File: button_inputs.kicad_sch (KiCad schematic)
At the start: 0 parts

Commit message: Add schematic for button inputs and I2C signal busses.
* Define 9x button inputs
* Define I2C parallel bus expanders used for FET output signals
  and button inputs
* Add (empty) schematic for 5V switching regulator.
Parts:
- added R? (x18): (no value), symbol Device:R_Small
- added SW? (x9): (no value), symbol Switch:SW_SPST
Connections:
- new net: R?.2, SW?.1 (A) (x9)
- new net GND: R?.1, R?.1, R?.1, R?.1, R?.1, R?.1, R?.1, R?.1, R?.1
- new net VCC: R?.1, R?.1, R?.1, R?.1, R?.1, R?.1, R?.1, R?.1, R?.1
- new net button0: R?.2, SW?.2 (B)
- new net button1: R?.2, SW?.2 (B)
- new net button2: R?.2, SW?.2 (B)
- new net button3: R?.2, SW?.2 (B)
- new net button4: R?.2, SW?.2 (B)
- new net button5: R?.2, SW?.2 (B)
- new net button6: R?.2, SW?.2 (B)
- new net button7: R?.2
- new net button8: R?.2, SW?.2 (B)
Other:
- note added: "3V3 logic through buttons"
- note added: "All buttons are active-low, normally-open circuit"

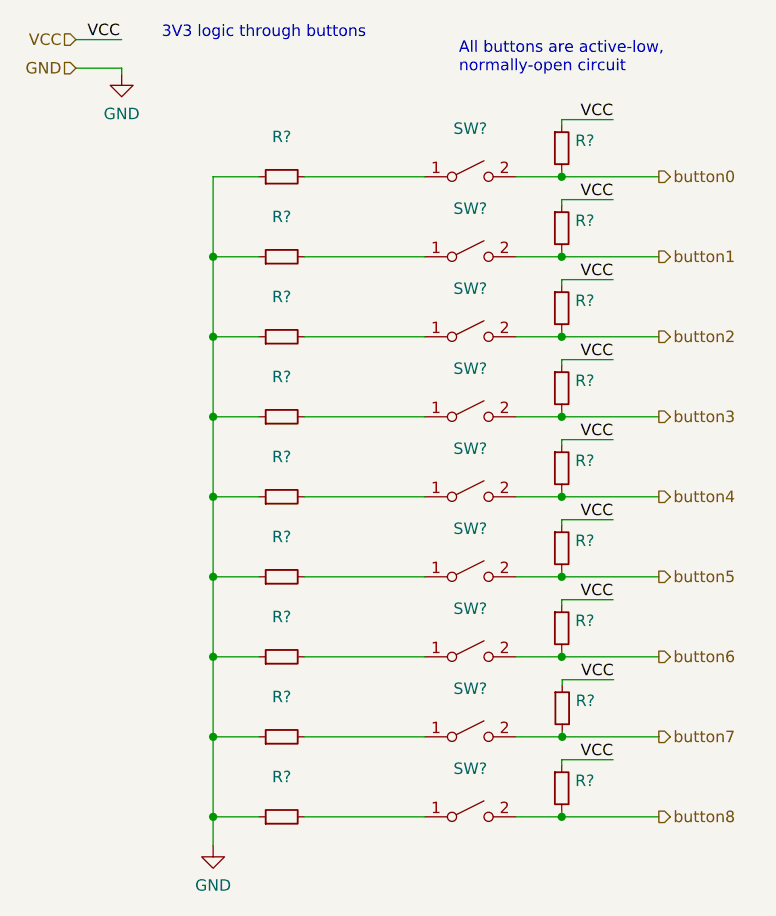
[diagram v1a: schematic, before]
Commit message: Sketch out ISL8117-driven 12V regulator.
Another candidate entry for on-board 12V regulation is to
build our own based on the reference schematic from the ISL8117
DC buck regulator controller datasheet.

Implemented (most of) this reference schematic here.
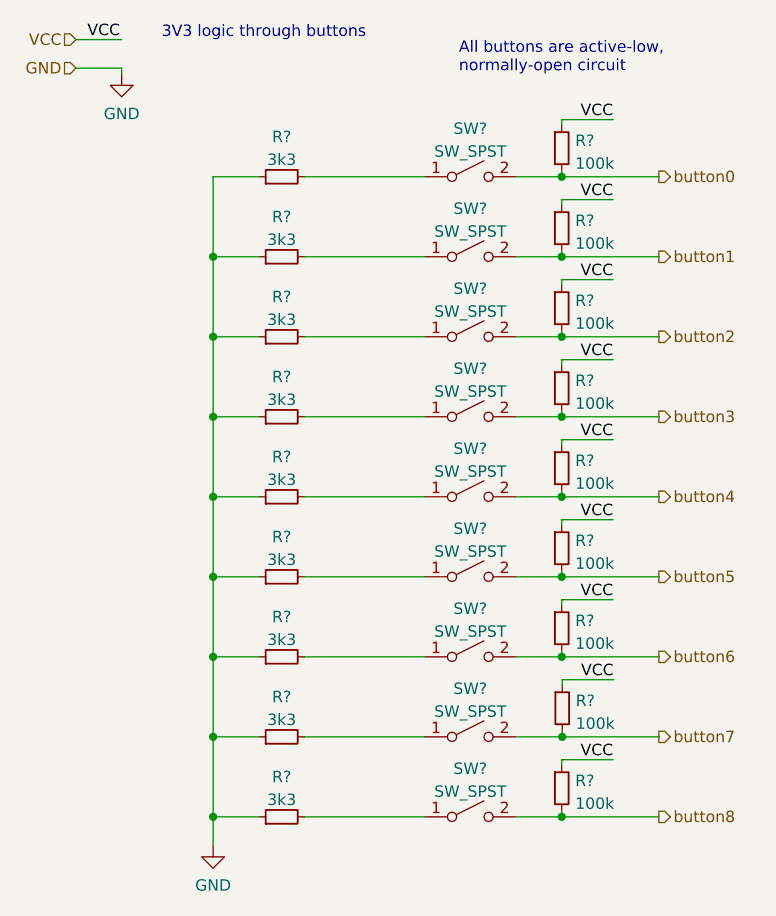
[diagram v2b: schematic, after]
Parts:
- R? (x9): value (none) -> 100k
- R? (x9): value (none) -> 3k3
- SW? (x9): value (none) -> SW_SPST
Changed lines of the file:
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@@
     (in_bom yes) (on_board yes) (fields_autoplaced)
     (property "Reference" "SW?" (id 0) (at 64.135 36.5592 0))
-    (property "Value" "" (id 1) (at 64.135 39.0961 0))
+    (property "Value" "SW_SPST" (id 1) (at 64.135 39.0961 0))
     (property "Footprint" "" (id 2) (at 64.135 41.91 0)
       (effects (font (size 1.27 1.27)) hide)
@@
       (effects (font (size 1.27 1.27)) (justify left))
     )
-    (property "Value" "" (id 1) (at 75.7936 49.3272 0)
+    (property "Value" "100k" (id 1) (at 75.7936 49.3272 0)
       (effects (font (size 1.27 1.27)) (justify left))
     )
@@
     (in_bom yes) (on_board yes)
     (property "Reference" "R?" (id 0) (at 43.18 37.4736 90))
-    (property "Value" "" (id 1) (at 43.18 40.0105 90))
+    (property "Value" "3k3" (id 1) (at 43.18 40.0105 90))
     (property "Footprint" "" (id 2) (at 43.18 41.91 0)
       (effects (font (size 1.27 1.27)) hide)
@@
     (in_bom yes) (on_board yes)
     (property "Reference" "R?" (id 0) (at 43.18 81.9236 90))
-    (property "Value" "" (id 1) (at 43.18 84.4605 90))
+    (property "Value" "3k3" (id 1) (at 43.18 84.4605 90))
     (property "Footprint" "" (id 2) (at 43.18 86.36 0)
       (effects (font (size 1.27 1.27)) hide)
@@
       (effects (font (size 1.27 1.27)) (justify left))
     )
-    (property "Value" "" (id 1) (at 75.8487 93.7772 0)
+    (property "Value" "100k" (id 1) (at 75.8487 93.7772 0)
       (effects (font (size 1.27 1.27)) (justify left))
     )
@@
     (in_bom yes) (on_board yes)
     (property "Reference" "R?" (id 0) (at 43.18 64.1436 90))
-    (property "Value" "" (id 1) (at 43.18 66.6805 90))
+    (property "Value" "3k3" (id 1) (at 43.18 66.6805 90))
     (property "Footprint" "" (id 2) (at 43.18 68.58 0)
       (effects (font (size 1.27 1.27)) hide)
@@
       (effects (font (size 1.27 1.27)) (justify left))
     )
-    (property "Value" "" (id 1) (at 75.7936 40.4372 0)
+    (property "Value" "100k" (id 1) (at 75.7936 40.4372 0)
       (effects (font (size 1.27 1.27)) (justify left))
     )
@@
     (in_bom yes) (on_board yes) (fields_autoplaced)
     (property "Reference" "SW?" (id 0) (at 64.135 81.0092 0))
-    (property "Value" "" (id 1) (at 64.135 83.5461 0))
+    (property "Value" "SW_SPST" (id 1) (at 64.135 83.5461 0))
     (property "Footprint" "" (id 2) (at 64.135 86.36 0)
       (effects (font (size 1.27 1.27)) hide)
@@
     (in_bom yes) (on_board yes) (fields_autoplaced)
     (property "Reference" "SW?" (id 0) (at 64.135 45.4492 0))
-    (property "Value" "" (id 1) (at 64.135 47.9861 0))
+    (property "Value" "SW_SPST" (id 1) (at 64.135 47.9861 0))
     (property "Footprint" "" (id 2) (at 64.135 50.8 0)
       (effects (font (size 1.27 1.27)) hide)
@@
     (in_bom yes) (on_board yes)
     (property "Reference" "R?" (id 0) (at 43.18 55.2536 90))
-    (property "Value" "" (id 1) (at 43.18 57.7905 90))
+    (property "Value" "3k3" (id 1) (at 43.18 57.7905 90))
     (property "Footprint" "" (id 2) (at 43.18 59.69 0)
       (effects (font (size 1.27 1.27)) hide)
@@
     (in_bom yes) (on_board yes) (fields_autoplaced)
     (property "Reference" "SW?" (id 0) (at 64.135 54.3392 0))
-    (property "Value" "" (id 1) (at 64.135 56.8761 0))
+    (property "Value" "SW_SPST" (id 1) (at 64.135 56.8761 0))
     (property "Footprint" "" (id 2) (at 64.135 59.69 0)
       (effects (font (size 1.27 1.27)) hide)
@@
     (in_bom yes) (on_board yes) (fields_autoplaced)
     (property "Reference" "SW?" (id 0) (at 64.135 89.8992 0))
-    (property "Value" "" (id 1) (at 64.135 92.4361 0))
+    (property "Value" "SW_SPST" (id 1) (at 64.135 92.4361 0))
     (property "Footprint" "" (id 2) (at 64.135 95.25 0)
       (effects (font (size 1.27 1.27)) hide)
@@
     (in_bom yes) (on_board yes) (fields_autoplaced)
     (property "Reference" "SW?" (id 0) (at 64.135 72.1192 0))
-    (property "Value" "" (id 1) (at 64.135 74.6561 0))
+    (property "Value" "SW_SPST" (id 1) (at 64.135 74.6561 0))
     (property "Footprint" "" (id 2) (at 64.135 77.47 0)
       (effects (font (size 1.27 1.27)) hide)
@@
       (effects (font (size 1.27 1.27)) (justify left))
     )
-    (property "Value" "" (id 1) (at 75.7936 58.2172 0)
+    (property "Value" "100k" (id 1) (at 75.7936 58.2172 0)
       (effects (font (size 1.27 1.27)) (justify left))
     )
@@
       (effects (font (size 1.27 1.27)) (justify left))
     )
-    (property "Value" "" (id 1) (at 75.7936 31.5472 0)
+    (property "Value" "100k" (id 1) (at 75.7936 31.5472 0)
       (effects (font (size 1.27 1.27)) (justify left))
     )
@@
     (in_bom yes) (on_board yes)
     (property "Reference" "R?" (id 0) (at 43.18 90.8136 90))
-    (property "Value" "" (id 1) (at 43.18 93.3505 90))
+    (property "Value" "3k3" (id 1) (at 43.18 93.3505 90))
     (property "Footprint" "" (id 2) (at 43.18 95.25 0)
       (effects (font (size 1.27 1.27)) hide)
@@
     (in_bom yes) (on_board yes)
     (property "Reference" "R?" (id 0) (at 43.18 73.0336 90))
-    (property "Value" "" (id 1) (at 43.18 75.5705 90))
+    (property "Value" "3k3" (id 1) (at 43.18 75.5705 90))
     (property "Footprint" "" (id 2) (at 43.18 77.47 0)
       (effects (font (size 1.27 1.27)) hide)
@@
     (in_bom yes) (on_board yes)
     (property "Reference" "R?" (id 0) (at 43.18 99.7036 90))
-    (property "Value" "" (id 1) (at 43.18 102.2405 90))
+    (property "Value" "3k3" (id 1) (at 43.18 102.2405 90))
     (property "Footprint" "" (id 2) (at 43.18 104.14 0)
       (effects (font (size 1.27 1.27)) hide)
@@
     (in_bom yes) (on_board yes) (fields_autoplaced)
     (property "Reference" "SW?" (id 0) (at 64.135 98.7892 0))
-    (property "Value" "" (id 1) (at 64.135 101.3261 0))
+    (property "Value" "SW_SPST" (id 1) (at 64.135 101.3261 0))
     (property "Footprint" "" (id 2) (at 64.135 104.14 0)
       (effects (font (size 1.27 1.27)) hide)
@@
       (effects (font (size 1.27 1.27)) (justify left))
     )
-    (property "Value" "" (id 1) (at 75.7936 102.6672 0)
+    (property "Value" "100k" (id 1) (at 75.7936 102.6672 0)
       (effects (font (size 1.27 1.27)) (justify left))
     )
@@
     (in_bom yes) (on_board yes) (fields_autoplaced)
     (property "Reference" "SW?" (id 0) (at 64.135 27.6692 0))
-    (property "Value" "" (id 1) (at 64.135 30.2061 0))
+    (property "Value" "SW_SPST" (id 1) (at 64.135 30.2061 0))
     (property "Footprint" "" (id 2) (at 64.135 33.02 0)
       (effects (font (size 1.27 1.27)) hide)
@@
     (in_bom yes) (on_board yes)
     (property "Reference" "R?" (id 0) (at 43.18 28.5836 90))
-    (property "Value" "" (id 1) (at 43.18 31.1205 90))
+    (property "Value" "3k3" (id 1) (at 43.18 31.1205 90))
     (property "Footprint" "" (id 2) (at 43.18 33.02 0)
       (effects (font (size 1.27 1.27)) hide)
@@
       (effects (font (size 1.27 1.27)) (justify left))
     )
-    (property "Value" "" (id 1) (at 75.7936 84.8872 0)
+    (property "Value" "100k" (id 1) (at 75.7936 84.8872 0)
       (effects (font (size 1.27 1.27)) (justify left))
     )
@@
       (effects (font (size 1.27 1.27)) (justify left))
     )
-    (property "Value" "" (id 1) (at 75.7936 67.1072 0)
+    (property "Value" "100k" (id 1) (at 75.7936 67.1072 0)
       (effects (font (size 1.27 1.27)) (justify left))
     )
@@
     (in_bom yes) (on_board yes)
     (property "Reference" "R?" (id 0) (at 43.18 46.3636 90))
-    (property "Value" "" (id 1) (at 43.18 48.9005 90))
+    (property "Value" "3k3" (id 1) (at 43.18 48.9005 90))
     (property "Footprint" "" (id 2) (at 43.18 50.8 0)
       (effects (font (size 1.27 1.27)) hide)
@@
     (in_bom yes) (on_board yes) (fields_autoplaced)
     (property "Reference" "SW?" (id 0) (at 64.135 63.2292 0))
-    (property "Value" "" (id 1) (at 64.135 65.7661 0))
+    (property "Value" "SW_SPST" (id 1) (at 64.135 65.7661 0))
     (property "Footprint" "" (id 2) (at 64.135 68.58 0)
       (effects (font (size 1.27 1.27)) hide)
@@
       (effects (font (size 1.27 1.27)) (justify left))
     )
-    (property "Value" "" (id 1) (at 75.7936 75.9972 0)
-      (effects (font (size 1.27 1.27)) (justify left))
-    )
+    (property "Value" "100k" (id 1) (at 75.7936 75.9972 0)
+      (effects (font (size 1.27 1.27)) (justify left))
+    )
